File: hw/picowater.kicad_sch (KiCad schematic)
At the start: 57 parts, among them J1 +12V, J10 Batt TP, J13 RJ45, J14 RJ45, J15 RJ45, J2 Power In, J3 12V TP, J4 UART, J6 JST-PH2 Bat, J7 GPIO2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

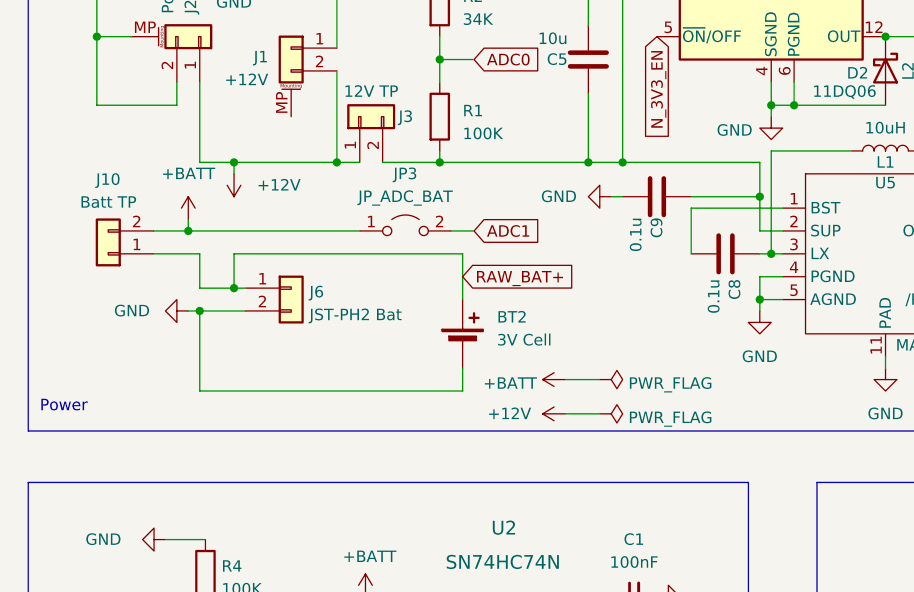
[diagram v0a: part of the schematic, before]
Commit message: [pcb] fix ADC + add internal connector for int. bat
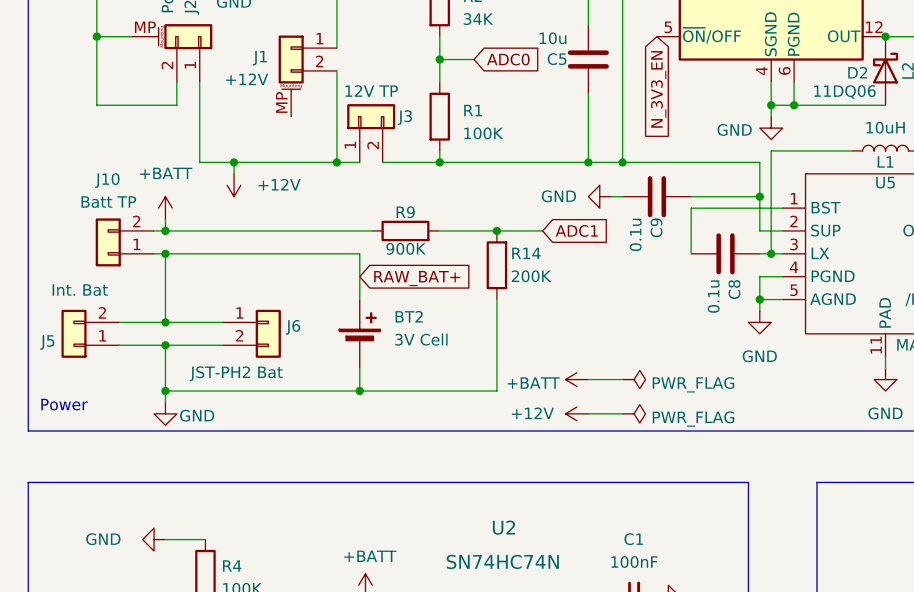
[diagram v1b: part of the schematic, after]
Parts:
- removed JP3: JP_ADC_BAT, Jumper:SolderJumper-2_P1.3mm_Open_Pad1.0x1.5mm, symbol Jumper:Jumper_2_Open
- added J5: Int. Bat, Connector_PinHeader_2.54mm:PinHeader_1x02_P2.54mm_Vertical, symbol Connector_Generic:Conn_01x02
- added R14: 200K, Resistor_SMD:R_0402_1005Metric, symbol Device:R
- added R9: 900K, Resistor_SMD:R_0402_1005Metric, symbol Device:R
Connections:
- net +BATT: now also R9.1
- net ADC1: now also R14.2, R9.2
- net GND: now also J5.1 (Pin_1), R14.1
- net RAW_BAT+: now also J5.2 (Pin_2)
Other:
- moved on the sheet: BT2, J6

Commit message: [fw] add support for batlvl2, temperature, add failsafe
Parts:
- R14: value 200K -> 900K
- R9: value 900K -> 200K
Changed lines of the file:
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@@
 			)
 		)
-		(property "Value" "900K"
+		(property "Value" "200K"
 			(at 58.42 104.902 90)
 			(effects
@@
 			)
 		)
-		(property "Value" "200K"
+		(property "Value" "900K"
 			(at 70.104 107.95 0)
 			(effects

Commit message: [pcb] fix diode polarity on relay
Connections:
- net +5V: now also D3.1 (K); no longer D3.2 (A)
- net at K1.1, Q2.3 (C): now also D3.2 (A); no longer D3.1 (K)
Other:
- moved on the sheet: D3
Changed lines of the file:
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@@
 	(symbol
 		(lib_id "Diode:1N4007")
-		(at 227.33 133.35 90)
+		(at 227.33 133.35 270)
 		(unit 1)
 		(exclude_from_sim no)
@@
 		(fields_autoplaced yes)
 		(property "Reference" "D3"
-			(at 229.87 132.08 90)
+			(at 229.87 132.0799 90)
 			(effects
 				(font
 					(size 1.27 1.27)
 				)
-				(justify right)
+				(justify left)
 			)
 		)
 		(property "Value" "1N4007"
-			(at 229.87 134.62 90)
+			(at 229.87 134.6199 90)
 			(effects
 				(font
 					(size 1.27 1.27)
 				)
-				(justify right)
+				(justify left)
 			)
 		)
 		(property "Footprint" "Diode_SMD:D_SOD-123"
-			(at 231.775 133.35 0)
+			(at 222.885 133.35 0)
 			(effects
 				(font
